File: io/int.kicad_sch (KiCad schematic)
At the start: 27 parts, among them J16 Conn_01x02, J18 Conn_02x05_Top_Bottom, Q2 Q_NPN, Q3 Q_PNP

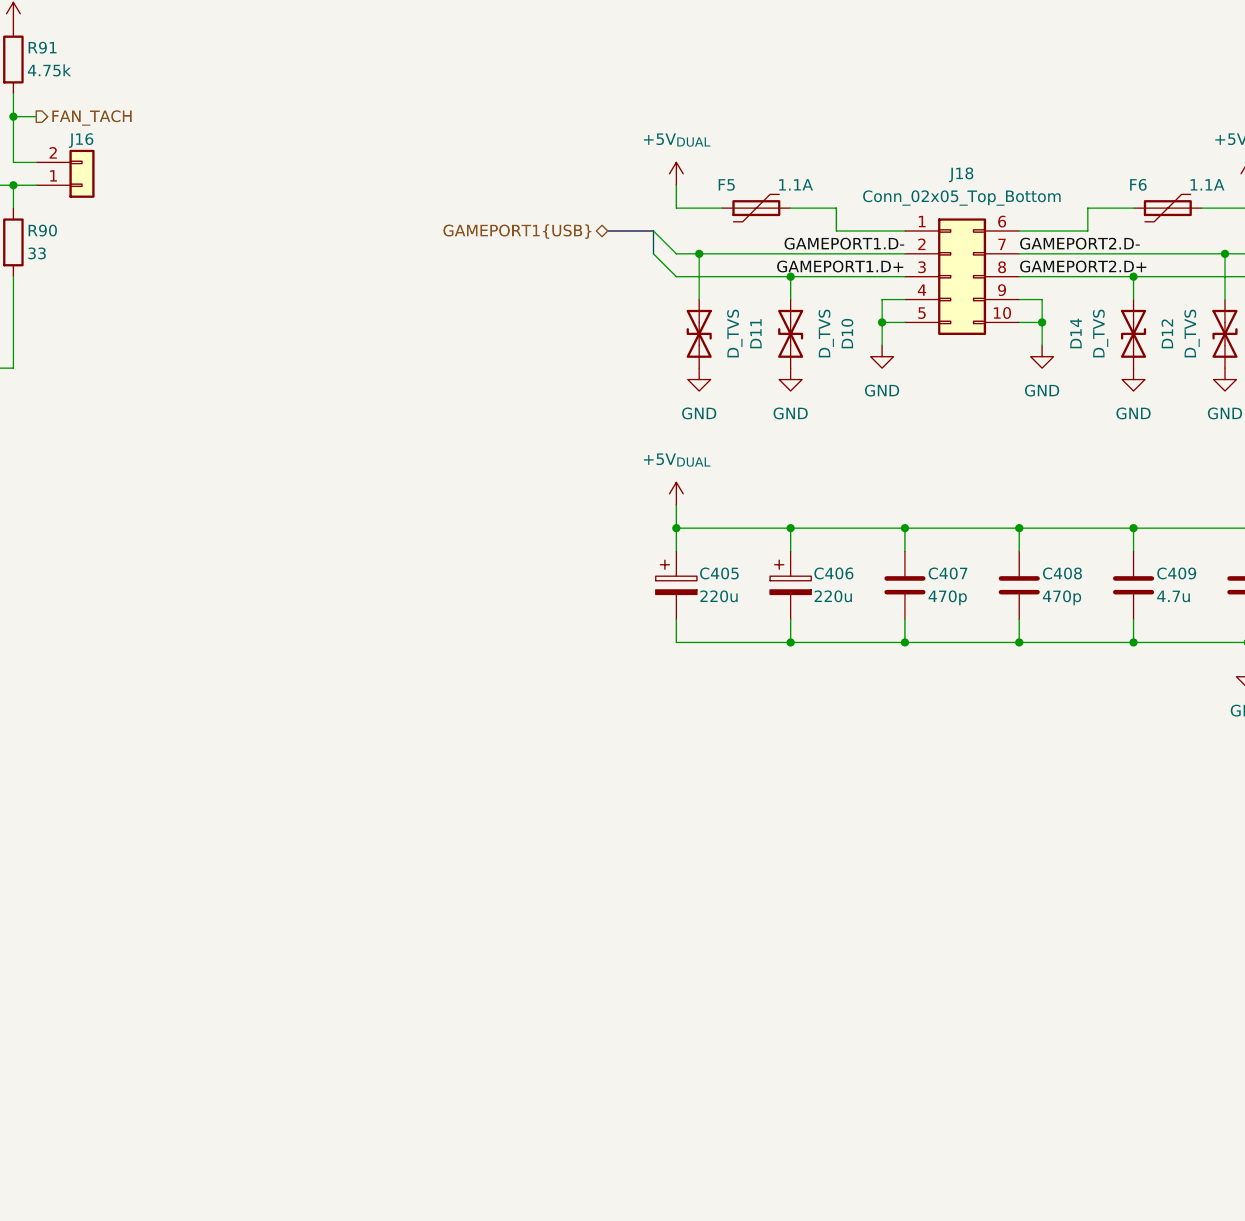
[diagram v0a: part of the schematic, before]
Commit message: Cleanup, SMC GPIO connections and Temperature sensing
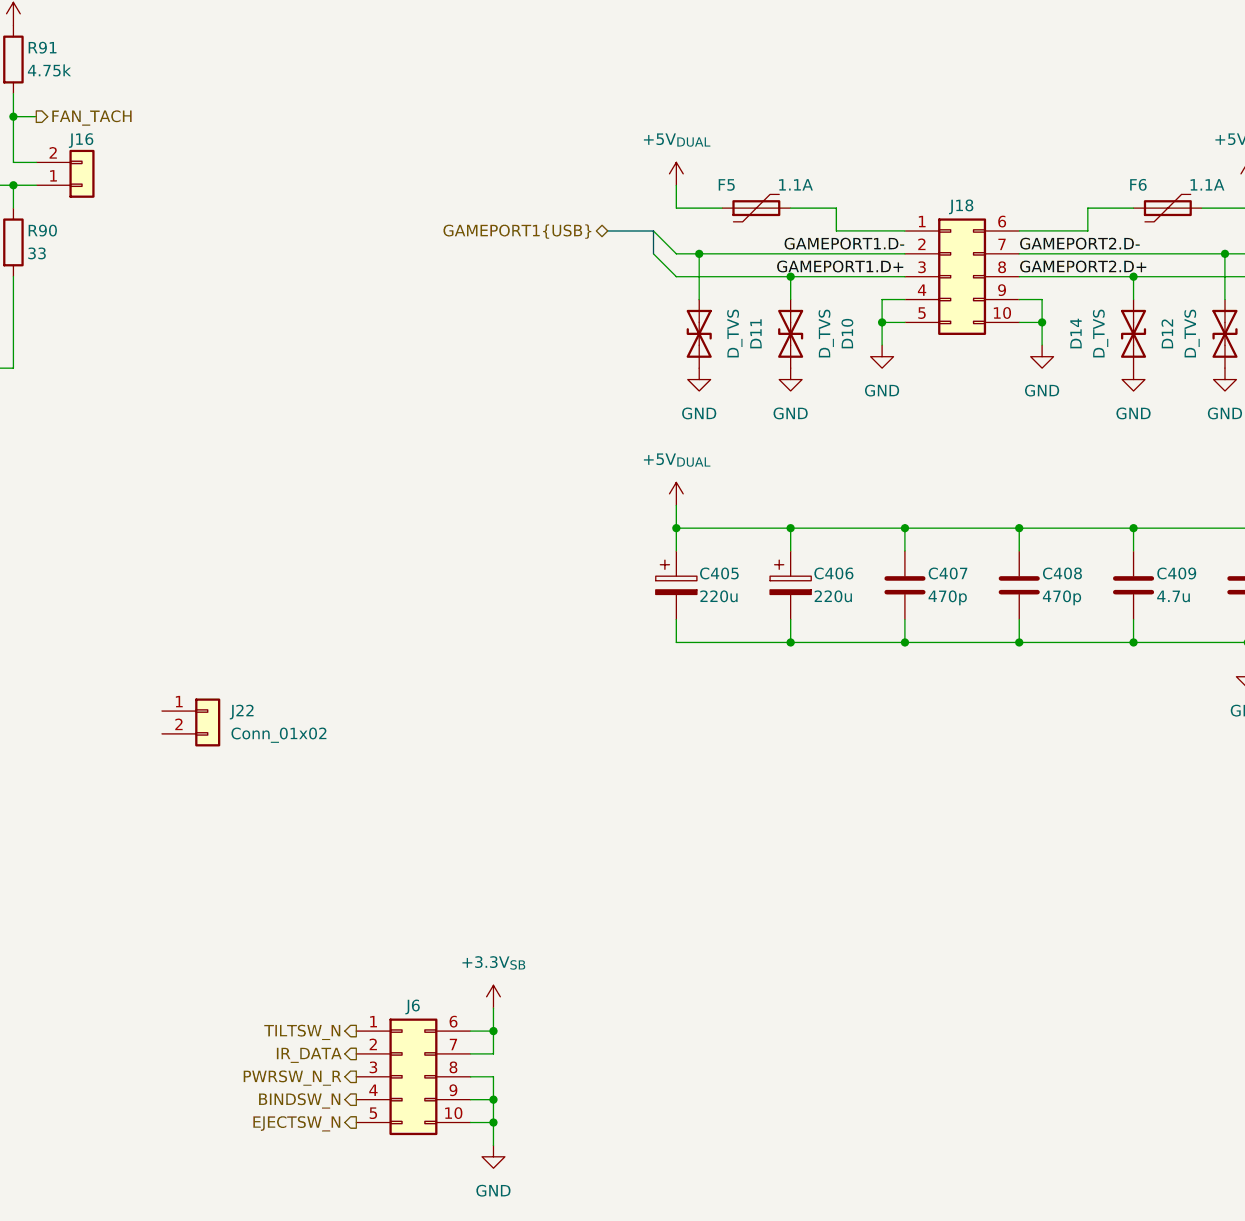
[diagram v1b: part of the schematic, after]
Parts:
- added J22: Conn_01x02, symbol Connector_Generic:Conn_01x02
- added J6: Conn_02x05_Top_Bottom, symbol Connector_Generic:Conn_02x05_Top_Bottom
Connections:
- net GND: now also J6.10 (Pin_10), J6.8 (Pin_8), J6.9 (Pin_9)
- new net +3.3V_{SB}: J6.6 (Pin_6), J6.7 (Pin_7)
- new net BINDSW_N: J6.4 (Pin_4)
- new net EJECTSW_N: J6.5 (Pin_5)
- new net IR_DATA: J6.2 (Pin_2)
- new net PWRSW_N_R: J6.3 (Pin_3)
- new net TILTSW_N: J6.1 (Pin_1)

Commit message: Internal Connectors
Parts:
- removed J22: Conn_01x02, symbol Connector_Generic:Conn_01x02
- removed J6: Conn_02x05_Top_Bottom, symbol Connector_Generic:Conn_02x05_Top_Bottom
- added C370, C372, C373: 470p, symbol Device:C
- added C371: 100u, symbol Device:C_Polarized
- added J1: Conn_02x11_Top_Bottom, symbol Connector_Generic:Conn_02x11_Top_Bottom
- added R127, R128, R129, R133, R134: 10k, symbol Device:R
- added R130, R131, R132: 100k, symbol Device:R
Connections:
- net +3.3V_{SB}: now also C370.1, C371.1, J1.1 (Pin_1), J1.19 (Pin_19), R130.1, R131.1, R132.1, R134.1
- net BINDSW_N: now also R129.1, R131.2
- net EJECTSW_N: now also C372.1, J1.7 (Pin_7), R127.1, R130.2
- net GND: now also C370.2, C371.2, C372.2, C373.2, J1.13 (Pin_13), J1.15 (Pin_15), J1.2 (Pin_2), J1.20 (Pin_20), J1.4 (Pin_4), J1.9 (Pin_9)
- net IR_DATA: now also J1.3 (Pin_3)
- net TILTSW_N: now also R133.2, R134.2
- new net: J1.16 (Pin_16), R128.1
- new net: J1.14 (Pin_14), R133.1
- new net: J1.5 (Pin_5), R129.2
- new net: J1.8 (Pin_8), R127.2
- new net BORONFPM.SCL: C373.1, J1.6 (Pin_6)
- new net BORONFPMPORT.D+: J1.17 (Pin_17)
- new net BORONFPMPORT.D-: J1.18 (Pin_18)
- new net PWRSW_N: R128.2, R132.2
- new net SPKR_DRIVE_N: J1.22 (Pin_22)
- new net SPKR_DRIVE_P: J1.21 (Pin_21)
- new net TRAY_OPEN: J1.10 (Pin_10)
- new net TRAY_STATUS: J1.11 (Pin_11)
- no-connect marks 0 -> 1
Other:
- moved on the sheet: C405, C406, C407, C408, C409, C410, D10, D11, D12, D14, F5, F6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

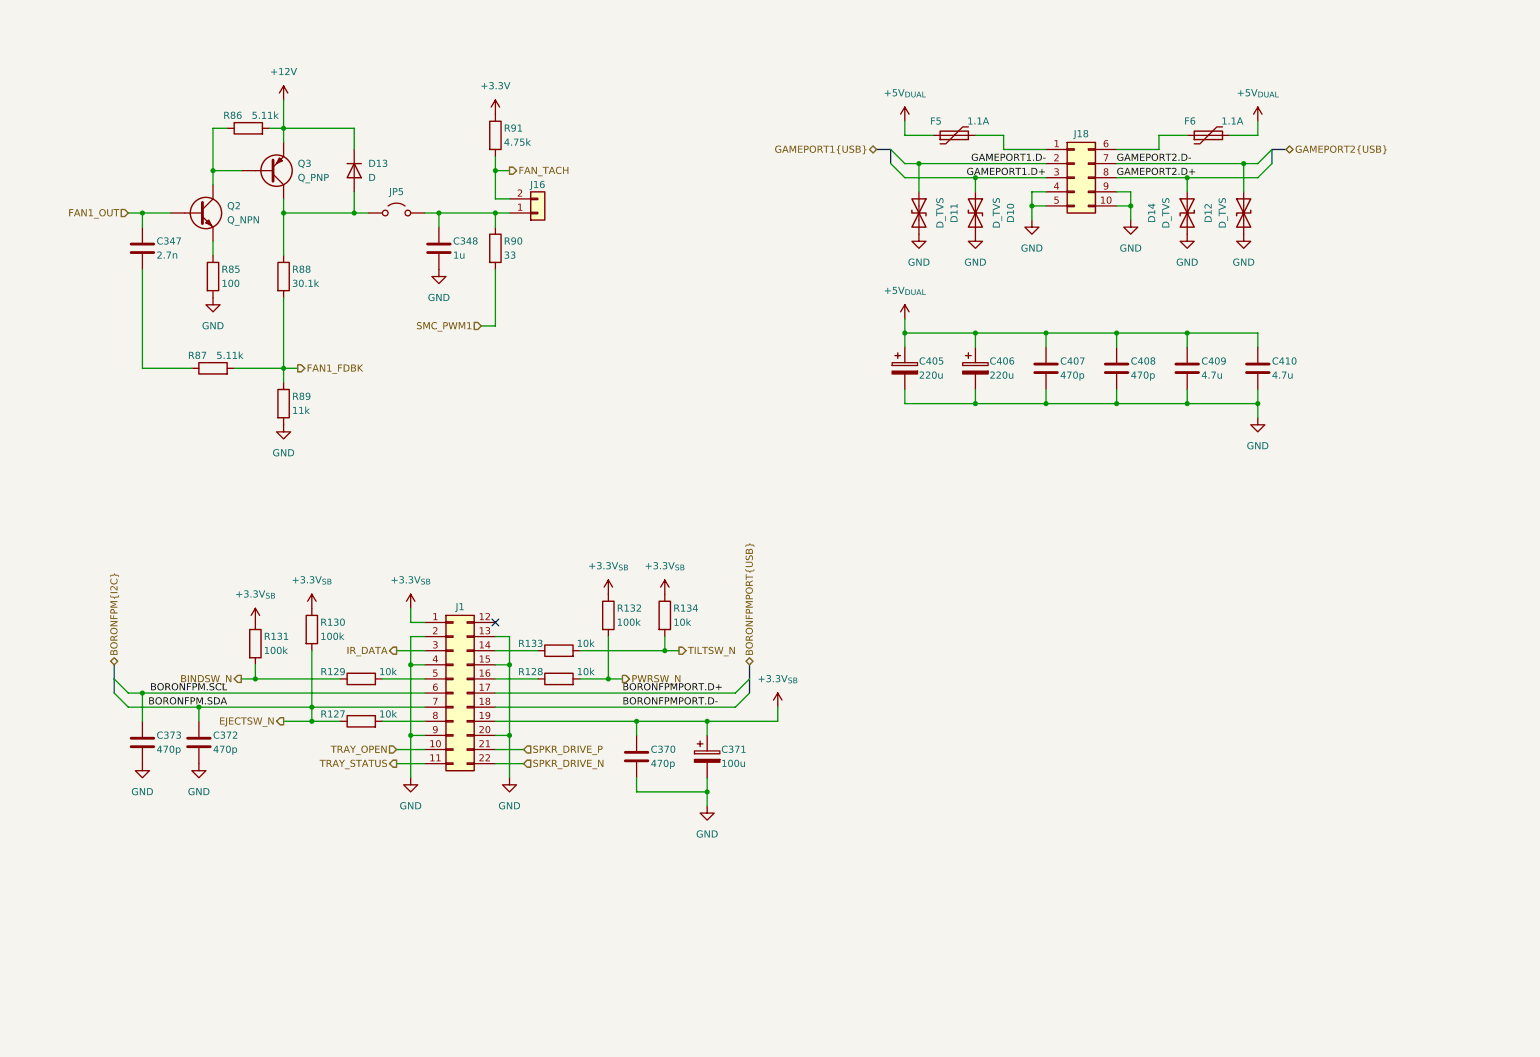
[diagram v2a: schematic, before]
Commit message: Nand Flash, Sata Connectors and removing (hopefully) unnecessary things
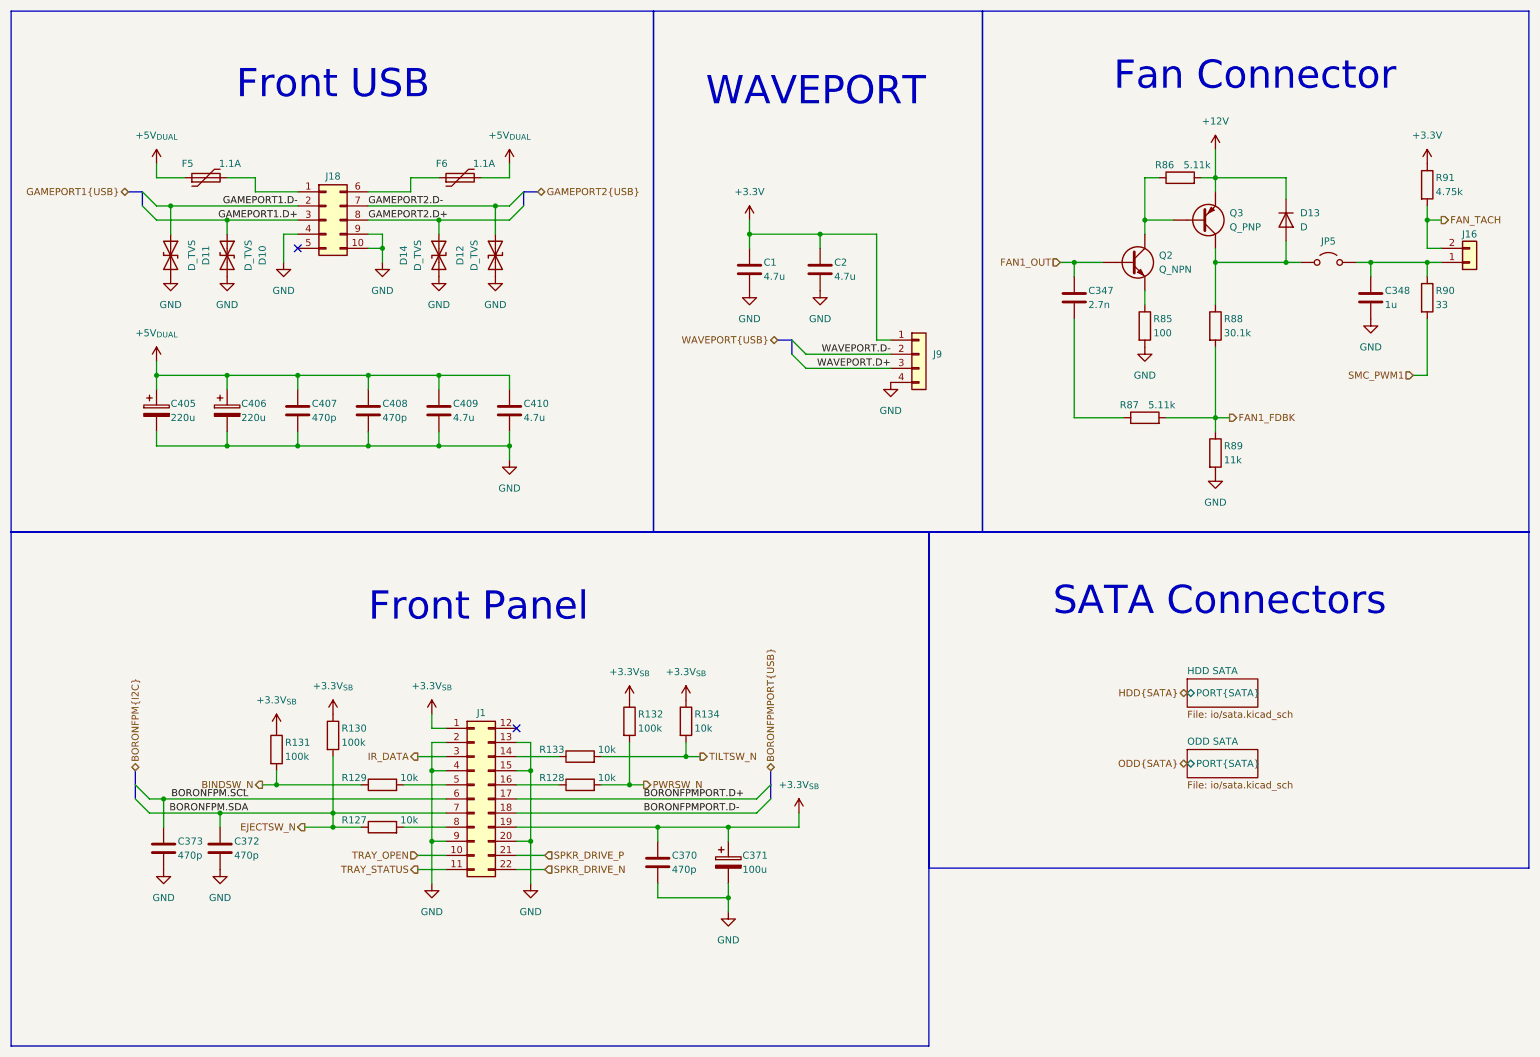
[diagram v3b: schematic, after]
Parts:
- added C1, C2: 4.7u, symbol Device:C
- added J9: Conn_01x04, symbol Connector_Generic:Conn_01x04
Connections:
- net +3.3V: now also C1.1, C2.1, J9.1 (Pin_1)
- net GND: now also C1.2, C2.2, J9.4 (Pin_4); no longer J18.5 (Pin_5)
- new net WAVEPORT.D+: J9.3 (Pin_3)
- new net WAVEPORT.D-: J9.2 (Pin_2)
- no-connect marks 1 -> 2
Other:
- added sheet HDD SATA (io/sata.kicad_sch)
- added sheet ODD SATA (io/sata.kicad_sch)
- note added: "Fan Connector"
- note added: "Front Panel"
- note added: "Front USB"
- note added: "SATA Connectors"
- note added: "WAVEPORT"
- moved on the sheet: C347, C348, C370, C371, C372, C373, C405, C406, C407, C408, C409, C410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

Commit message: Sata schematic location fix
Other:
- sheet HDD SATA: file io/sata.kicad_sch -> sata.kicad_sch
- sheet ODD SATA: file io/sata.kicad_sch -> sata.kicad_sch
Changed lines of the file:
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@@
 			)
 		)
-		(property "Sheetfile" "io/sata.kicad_sch"
+		(property "Sheetfile" "sata.kicad_sch"
 			(at 223.52 137.7446 0)
 			(effects
@@
 			)
 		)
-		(property "Sheetfile" "io/sata.kicad_sch"
+		(property "Sheetfile" "sata.kicad_sch"
 			(at 223.52 150.4446 0)
 			(effects
